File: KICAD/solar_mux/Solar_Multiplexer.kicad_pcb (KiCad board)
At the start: 2 copper layers, 205 x 190 mm, 38 parts, among them J1 Conn_01x14, J2 Conn_02x06_Odd_Even, J3 Conn_02x06_Odd_Even, U1 ASSR-1611, U10 ASSR-1611, U11 ASSR-1611, U12 ASSR-1611, U13 ASSR-1611, U14 ASSR-1611, U15 ASSR-1611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

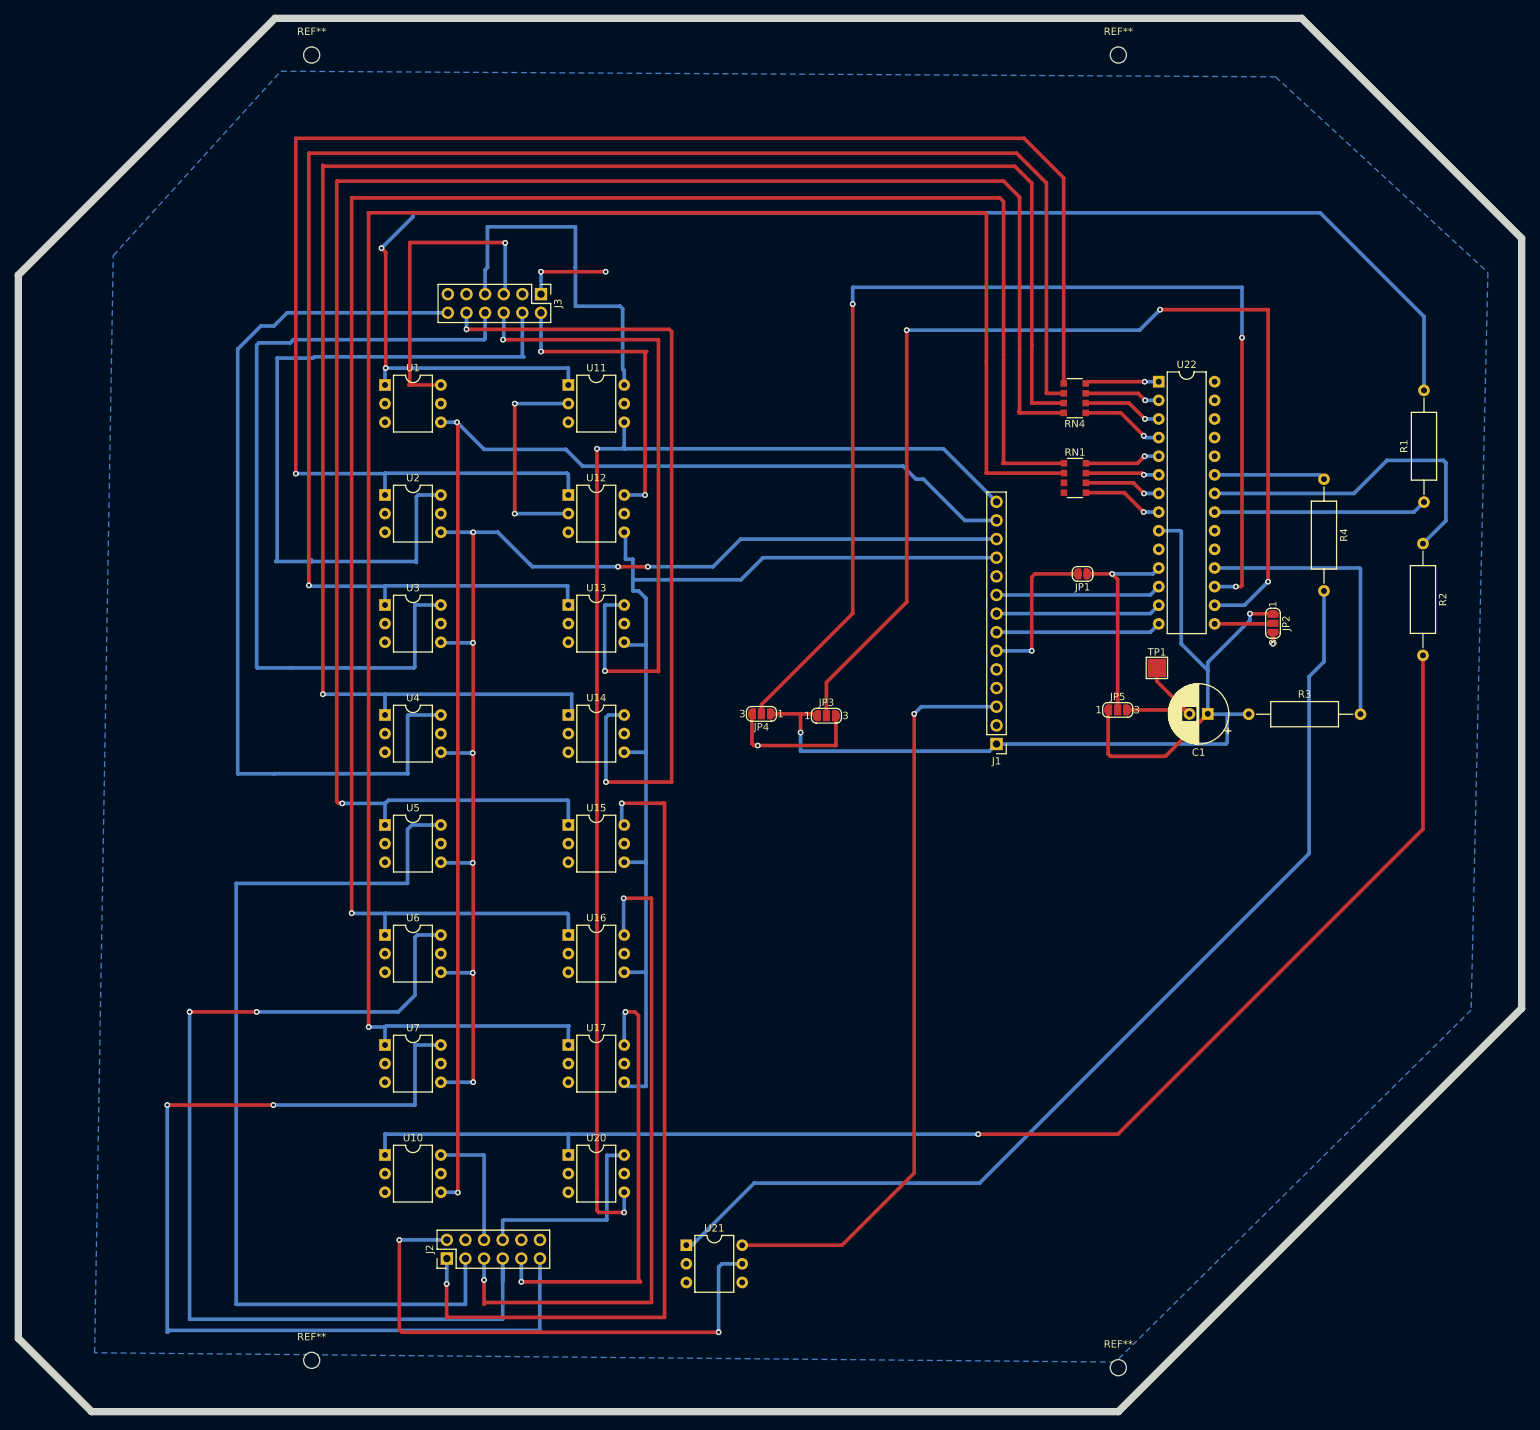
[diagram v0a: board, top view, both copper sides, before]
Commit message: Chanign track sizes and re producing drill files
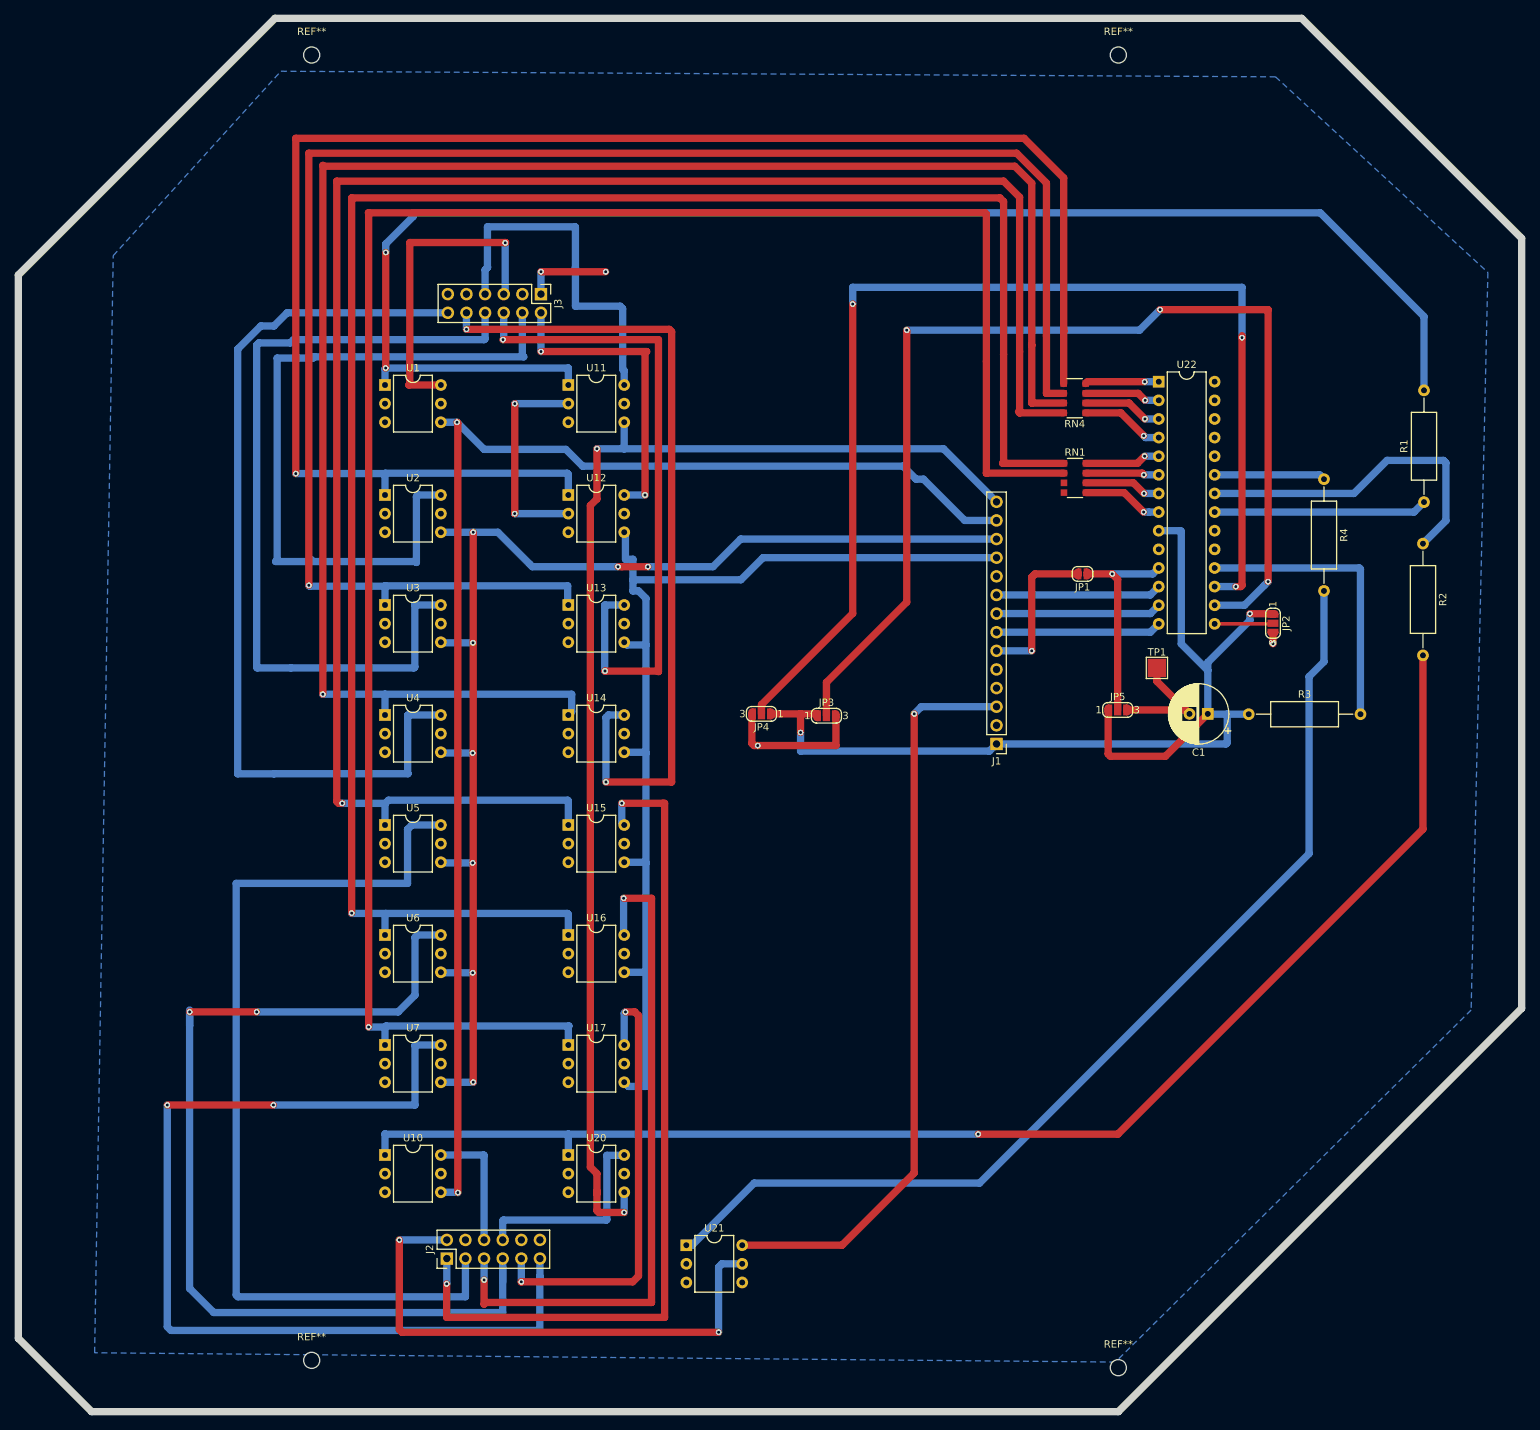
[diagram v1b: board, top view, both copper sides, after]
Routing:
- net /V4: track 130.4 -> 128.2 mm
- net /V5: track 138.4 -> 136.5 mm
- net /I6: track 62.4 -> 61.6 mm
- net I-: track 172.2 -> 172.9 mm
- net /V6: track 137.9 -> 137.2 mm

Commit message: Changing Via sizes and track widths
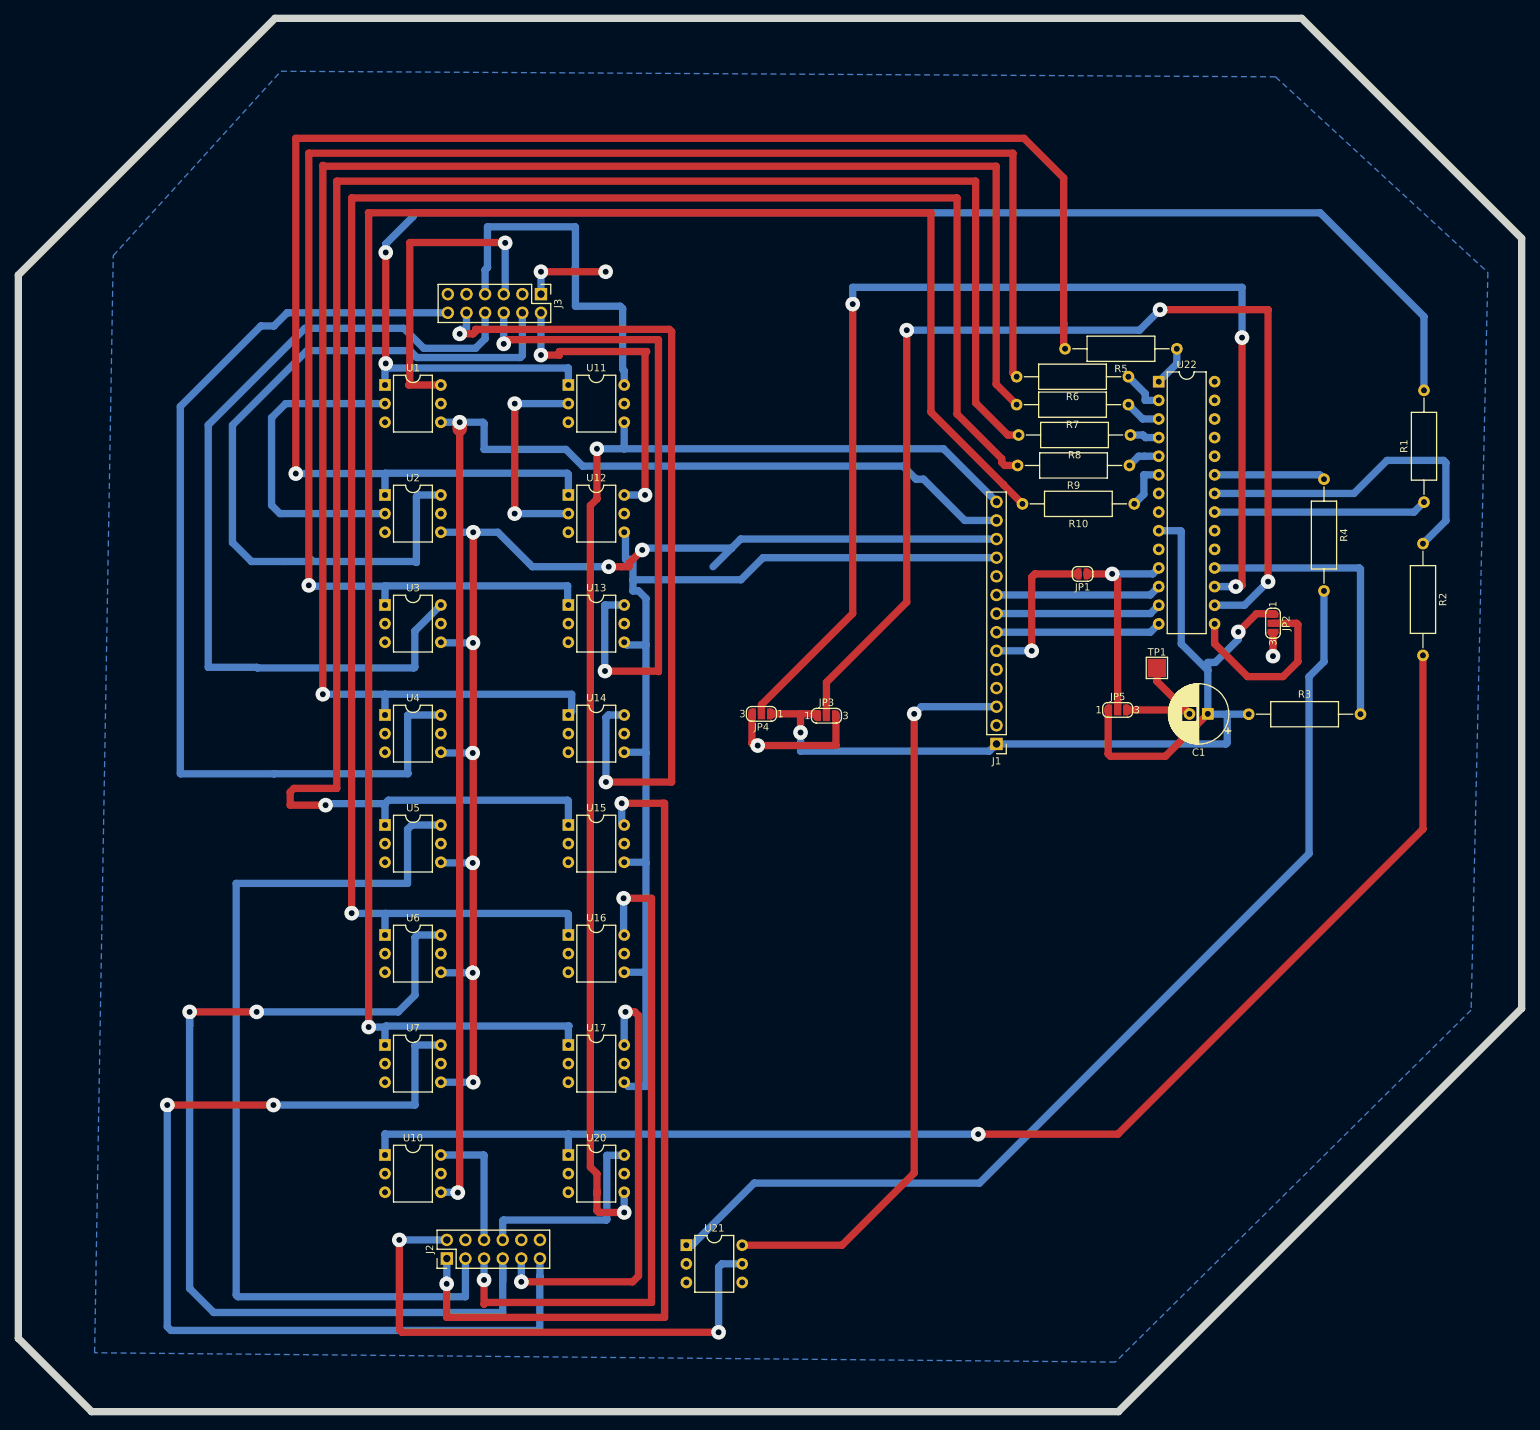
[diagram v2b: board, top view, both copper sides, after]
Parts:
- removed REF** (x4): MountingHole_2.2mm_M2, MountingHole:MountingHole_2.2mm_M2
- removed RN1, RN4: 330R, Resistor_SMD:R_Array_Convex_4x1206
- added R10: 330R, Resistor_THT:R_Axial_DIN0309_L9.0mm_D3.2mm_P15.24mm_Horizontal, F.Cu at (-197.8, 136.2)
- added R5: 330R, Resistor_THT:R_Axial_DIN0309_L9.0mm_D3.2mm_P15.24mm_Horizontal, F.Cu at (-192.0, 115.1)
- added R6: 330R, Resistor_THT:R_Axial_DIN0309_L9.0mm_D3.2mm_P15.24mm_Horizontal, F.Cu at (-198.6, 118.9)
- added R7: 330R, Resistor_THT:R_Axial_DIN0309_L9.0mm_D3.2mm_P15.24mm_Horizontal, F.Cu at (-198.6, 122.7)
- added R8: 330R, Resistor_THT:R_Axial_DIN0309_L9.0mm_D3.2mm_P15.24mm_Horizontal, F.Cu at (-198.3, 126.8)
- added R9: 330R, Resistor_THT:R_Axial_DIN0309_L9.0mm_D3.2mm_P15.24mm_Horizontal, F.Cu at (-198.5, 131.0)
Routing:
- net GND: track 79.5 -> 125.8 mm
- net A0: track 7.99 -> 25.3 mm
- net /V3: track 124.4 -> 135.4 mm
- net Net-(U22-Pad8): track 11.0 -> 0.00 mm, vias 1 -> 0
- net Net-(U22-Pad7): track 10.5 -> 0.00 mm, vias 1 -> 0
- net /P5: track 266.1 -> 256.4 mm
- net /P6: track 273.8 -> 265.1 mm
- net /P4: track 252.6 -> 260.6 mm
- net Net-(R8-Pad1): track 11.4 -> 4.36 mm, vias 1 -> 0
- net /V2: track 112.7 -> 119.6 mm
- net /P2: track 232.8 -> 226.2 mm
- net /P3: track 244.0 -> 237.5 mm
- net Net-(R7-Pad1): track 10.9 -> 4.94 mm, vias 1 -> 0
- net Net-(R9-Pad1): track 10.3 -> 4.52 mm, vias 1 -> 0
- net /V1: track 100.0 -> 105.4 mm
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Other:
- net class Default: clearance 0.2 -> 0.25; via_dia 0.8 -> 2; via_drill 0.4 -> 0.8
- rule trace_clearance: 0.2 -> 0.25
- rule via_min_size: 0.4 -> 1.9
